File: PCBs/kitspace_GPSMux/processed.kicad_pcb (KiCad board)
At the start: 2 copper layers, 20 x 26 mm, 20 parts, among them P1 ICSP, P2 GPS1, P3 GPS2, P4 LLU, U1 CY8C27143-24PXI, U2 ADM3101EARQZ

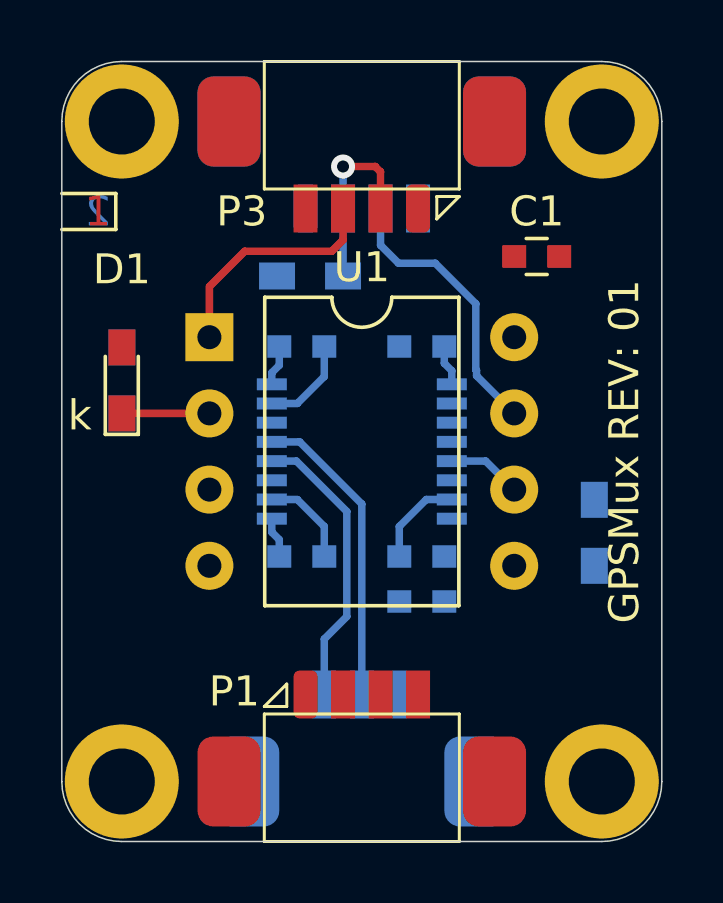
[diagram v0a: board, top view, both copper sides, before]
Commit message: recheck all circuits and clean up fill zone by rerouting the nets using freerouting and manually
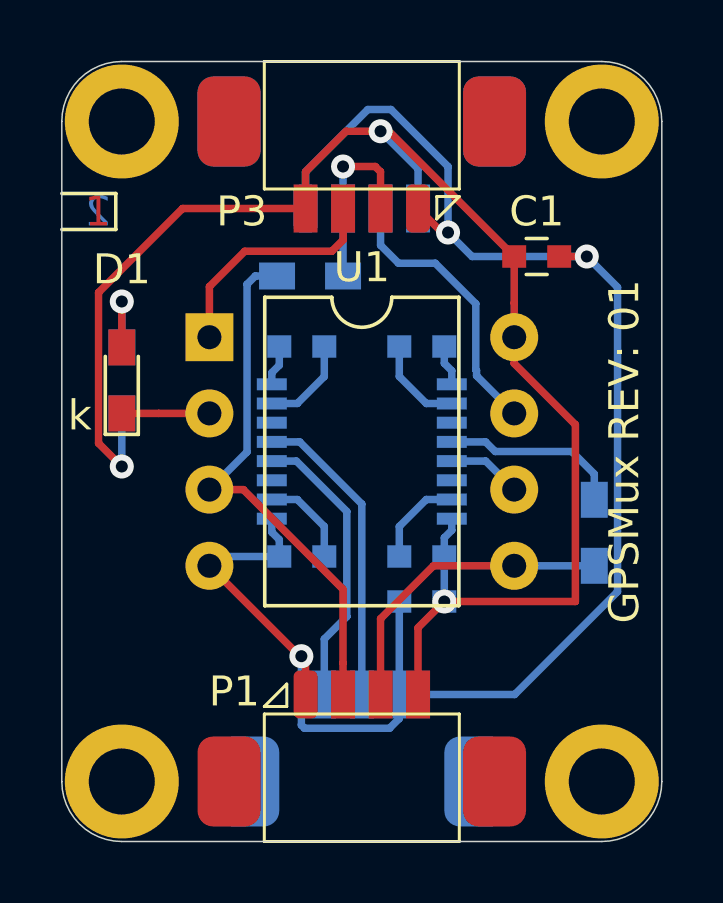
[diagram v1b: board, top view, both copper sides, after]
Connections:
- C1 pad 1: (no net) -> +3.3V
- C1 pad 2: (no net) -> GND
- C2 pad 2: (no net) -> Net-(C2-Pad2)
- C3 pad 2: (no net) -> +3.3V
- C4 pad 1: (no net) -> +3.3V
- C4 pad 2: (no net) -> GND
- D1 pad 2: (no net) -> Net-(D1-Pad2)
- P1 pad 1: (no net) -> GND
- P1 pad 2: (no net) -> I2C_SCL
- P1 pad 3: (no net) -> I2C_SDA
- P1 pad 4: (no net) -> +3.3V
- P2 pad 1: (no net) -> GND
- P2 pad 4: (no net) -> +3.3V
- P3 pad 1: (no net) -> GND
- P3 pad 4: (no net) -> +3.3V
- P4 pad 1: (no net) -> GND
- R1 pad 1: (no net) -> Net-(D1-Pad2)
- R1 pad 2: (no net) -> +3.3V
- R2 pad 1: (no net) -> I2C_SDA
- R2 pad 2: (no net) -> RX
- R3 pad 2: (no net) -> I2C_SCL
- U1 pad 3: (no net) -> I2C_SCL
- U1 pad 4: (no net) -> GND
- U1 pad 5: (no net) -> I2C_SDA
- U1 pad 8: (no net) -> +3.3V
- U2 pad 2: (no net) -> Net-(C2-Pad2)
- U2 pad 4: (no net) -> RX
- U2 pad 8: (no net) -> +3.3V
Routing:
- net GND: track 1.36 -> 56.3 mm, vias 0 -> 3
- net +3.3V: track 0.00 -> 52.6 mm, vias 0 -> 3
- net I2C_SCL: track 0.00 -> 17.8 mm
- net I2C_SDA: track 0.00 -> 10.4 mm
- net RX: track 0.00 -> 6.09 mm
- net Net-(D1-Pad2): track 0.00 -> 2.93 mm, vias 0 -> 1
- net Net-(C2-Pad2): track 0.00 -> 2.62 mm

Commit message: clean psbc that are missed before
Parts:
- renumbered REF** to REF**_2, REF** to REF**_3, REF** to REF**_4
